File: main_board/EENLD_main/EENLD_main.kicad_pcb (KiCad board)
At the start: 4 copper layers, 130 x 68 mm, 130 parts, among them J101 Conn_01x06_Pin, J102 Conn_01x02_Pin, J201 Conn_01x02_Socket, J301 Conn_01x02_Socket, J401 Conn_01x02_Socket, J501 Conn_01x02_Socket, J601 Conn_01x02_Socket, Q201 AO3401A, Q301 AO3400A, Q401 AO3400A, Q501 AO3400A, Q601 AO3400A, SW101 SW_Push, SW102 SW_SPDT, SW201 SW_SPDT, U101 Pico, U201 TPS25200DRVR, U301 AD5160BRJZ5, U302 RT9187QV, U401 AD5160BRJZ5, U402 RT9187QV, U501 AD5160BRJZ5, U502 RT9187QV, U601 AD5160BRJZ5, U602 RT9187QV, U701 74HC4052, U702 TLV9002, U703 TLV9002

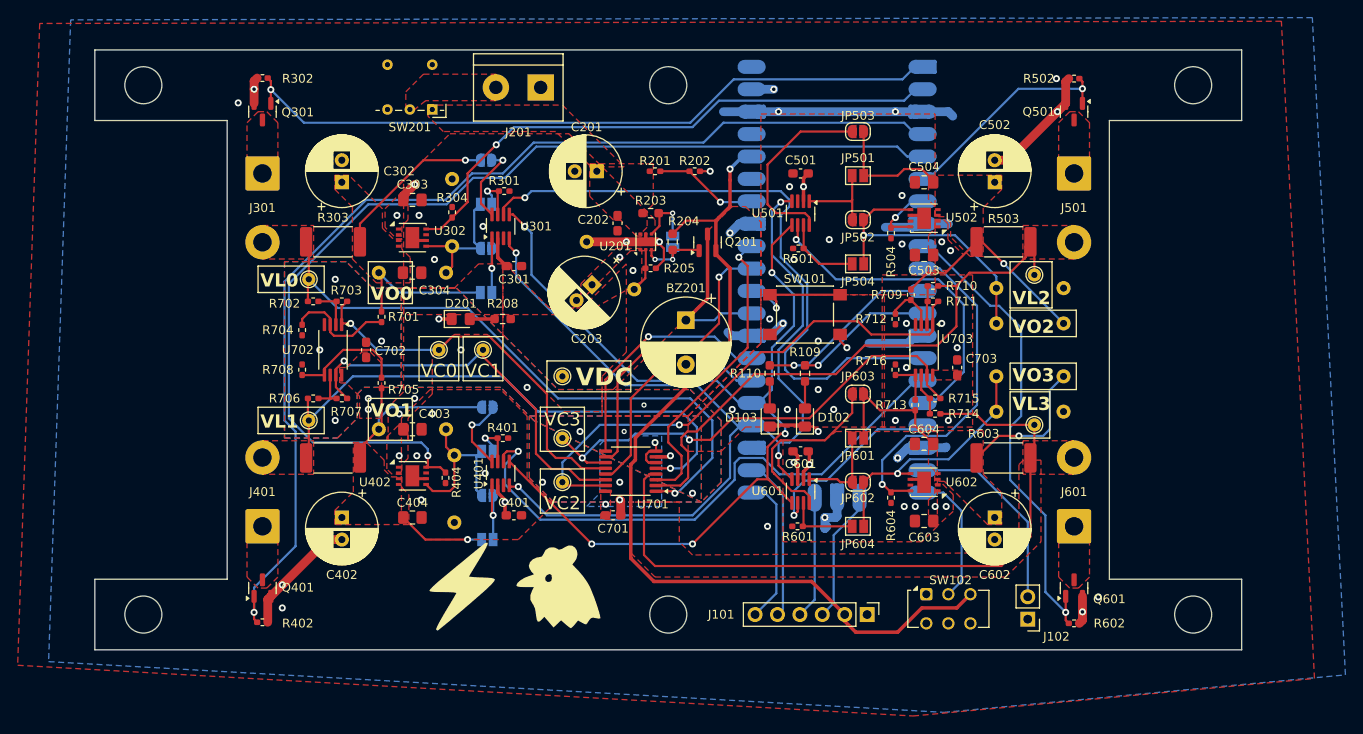
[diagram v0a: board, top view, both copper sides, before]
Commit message: added midi2array
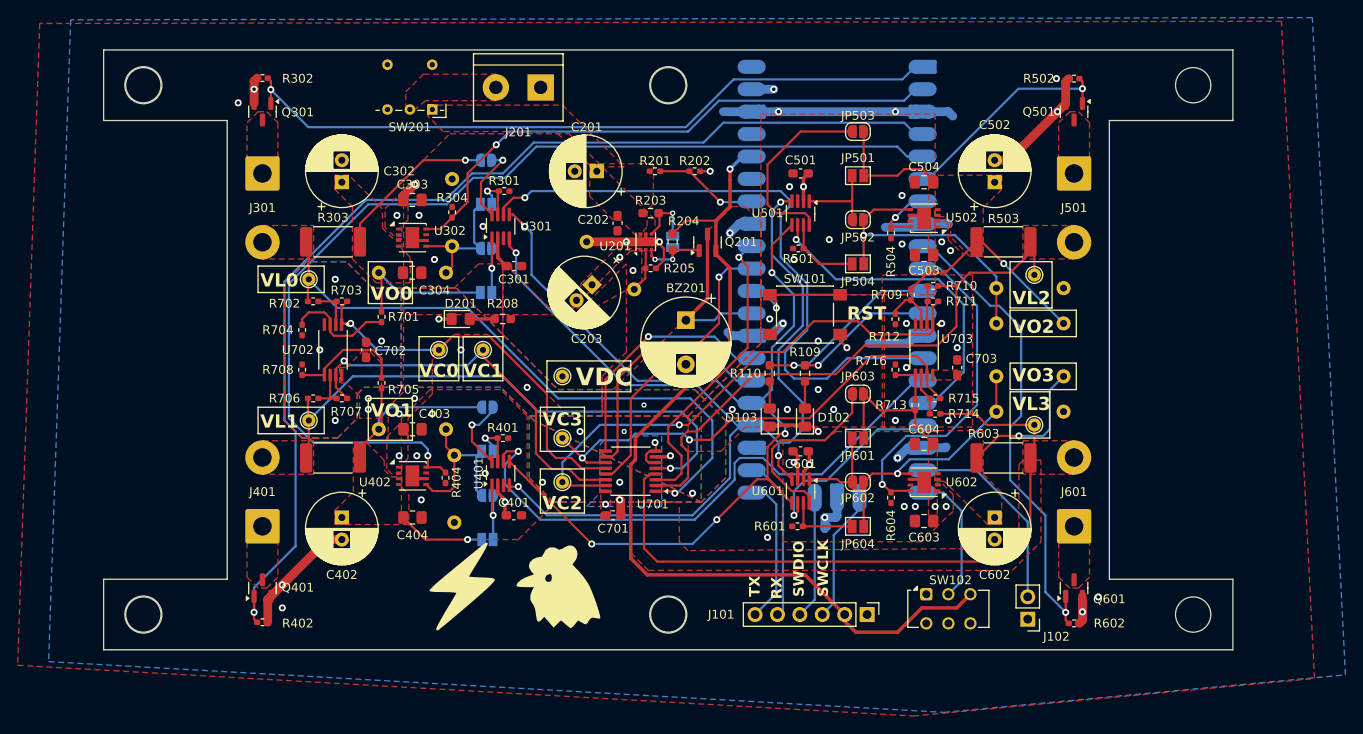
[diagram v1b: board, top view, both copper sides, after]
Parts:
- added REF**: MountingHole_4mm, MountingHole:MountingHole_4mm, F.Cu at (174.5, 114.0)
- added REF**: MountingHole_4mm, MountingHole:MountingHole_4mm, F.Cu at (55.5, 114.0)
- added REF**: MountingHole_4mm, MountingHole:MountingHole_4mm, F.Cu at (115.0, 54.0)
- added REF**: MountingHole_4mm, MountingHole:MountingHole_4mm, F.Cu at (174.5, 54.0)
- added REF**: MountingHole_4mm, MountingHole:MountingHole_4mm, F.Cu at (115.0, 114.0)
- added REF**: MountingHole_4mm, MountingHole:MountingHole_4mm, F.Cu at (55.5, 54.0)
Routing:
- net /VL3: track 79.9 -> 79.1 mm
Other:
- board size 130 x 68 mm -> 128 x 68 mm
- board text added: "1"
- board text added: "2"
- board text added: "3"
- board text added: "O"
- board text added: "R Ilim"
- board text added: "RST"
- board text added: "RX"
- board text added: "Round for Divider Rectangle for Rheostat"
- board text added: "SWCLK"
- board text added: "SWDIO"
- board text added: "Short EN and ~{FAULT}"
- board text added: "TX"
